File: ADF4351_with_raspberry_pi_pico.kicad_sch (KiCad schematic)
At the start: 0 parts

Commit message: wip ディスプレイとの接続、PLLとの接続は確定。制御用のボタン部分の作成を要する。
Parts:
- added A1: RaspberryPi_Pico, Module:RaspberryPi_Pico_Common_Unspecified, symbol MCU_Module:RaspberryPi_Pico
- added J1, J3: B4B-XH-A_LF__SN_, digikey-footprints:PinHeader_1x4_P2.5mm_Drill1.1mm, symbol dk_Rectangular-Connectors-Headers-Male-Pins:B4B-XH-A_LF__SN_
- added J2: 302-S101, digikey-footprints:PinHeader_2x5_P2.54mm_Drill1.2mm, symbol dk_Rectangular-Connectors-Headers-Male-Pins:302-S101
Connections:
- new net +3.3V: A1.36 (3V3), J1.1, J2.2
- new net +5V: A1.40 (VBUS), J3.1
- new net CE: A1.7 (GPIO5), J2.3
- new net CLK: A1.4 (GPIO2), J2.7
- new net DAT: A1.5 (GPIO3), J2.6
- new net GND: A1.13 (GND), A1.18 (GND), A1.23 (GND), A1.28 (GND), A1.3 (GND), A1.38 (GND), A1.8 (GND), J1.2, J2.1, J2.4, J3.4
- new net I2C0_SCL: A1.22 (GPIO17), J1.3
- new net I2C0_SDA: A1.21 (GPIO16), J1.4
- new net LD: A1.11 (GPIO8), J2.9
- new net LE: A1.10 (GPIO7), J2.5
- new net MUX: A1.6 (GPIO4), J2.8
- new net PDR: A1.9 (GPIO6), J2.10
- new net UART0_RX: A1.2 (GPIO1), J3.3
- new net UART0_TX: A1.1 (GPIO0), J3.2

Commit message: 回路図完成
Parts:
- added J4: Conn_01x03_Socket, Connector_PinSocket_2.54mm:PinSocket_1x03_P2.54mm_Vertical, symbol Connector:Conn_01x03_Socket
- added J5: Conn_01x05_Socket, Connector_PinSocket_2.54mm:PinSocket_1x03_P2.54mm_Vertical, symbol Connector:Conn_01x05_Socket
- added R1, R2: NC, Resistor_SMD:R_0603_1608Metric_Pad0.98x0.95mm_HandSolder, symbol Device:R_Small
- added R3, R4, R5: 1k, Resistor_SMD:R_0603_1608Metric_Pad0.98x0.95mm_HandSolder, symbol Device:R_Small
- added R6: 10k, Resistor_SMD:R_0603_1608Metric_Pad0.98x0.95mm_HandSolder, symbol Device:R_Small
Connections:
- net +3.3V: now also R1.1, R2.1
- net +5V: now also J5.5 (Pin_5)
- net GND: now also J4.2 (Pin_2), R6.1
- net I2C0_SCL: now also R1.2
- net I2C0_SDA: now also R2.2
- net Encoder_A: now reaches A1.14 (GPIO10)
- net Encoder_A: now also J4.1 (Pin_1)
- net Encoder_B: now reaches A1.15 (GPIO11)
- net Encoder_B: now also J4.3 (Pin_3)
- net Encoder_PUSH: now reaches A1.24 (GPIO18)
- net Encoder_PUSH: now also J5.3 (Pin_3), R6.2
- net Encoder_LED_RED: now reaches A1.25 (GPIO19)
- net Encoder_LED_RED: now also R3.1
- net Encoder_LED_GREEN: now reaches A1.26 (GPIO20)
- net Encoder_LED_GREEN: now also R4.1
- net Encoder_LED_BLUE: now reaches A1.27 (GPIO21)
- net Encoder_LED_BLUE: now also R5.1
- new net: J5.1 (Pin_1), R3.2
- new net: J5.4 (Pin_4), R5.2
- new net: J5.2 (Pin_2), R4.2
- no-connect marks 0 -> 13
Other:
- note added: "プルアップ用 対象のモジュール基板にプルアップがある場合は付けない"
- note added: "５VじゃないとLEDを駆動出来ない。 ラズピコが耐える事に期待する"
- moved on the sheet: J1, J2, J3

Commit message: マウントホールを追加
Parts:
- added H1, H2, H3, H4: MountingHole_Pad_MP, MountingHole:MountingHole_3.2mm_M3_Pad_Via, symbol Mechanical:MountingHole_Pad_MP
- J5: footprint Connector_PinSocket_2.54mm:PinSocket_1x03_P2.54mm_Vertical -> Connector_PinSocket_2.54mm:PinSocket_1x05_P2.54mm_Vertical
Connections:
- net GND: now also H1.MP, H2.MP, H3.MP, H4.MP
- no-connect marks 13 -> 14

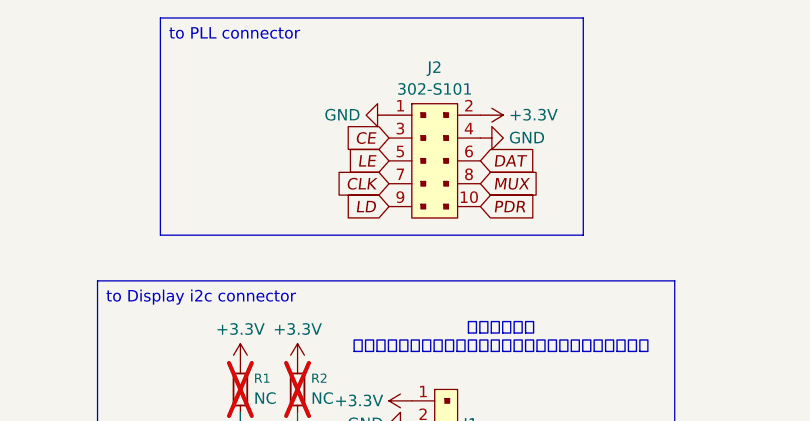
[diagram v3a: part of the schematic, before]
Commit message: fix 5*2 connector pin
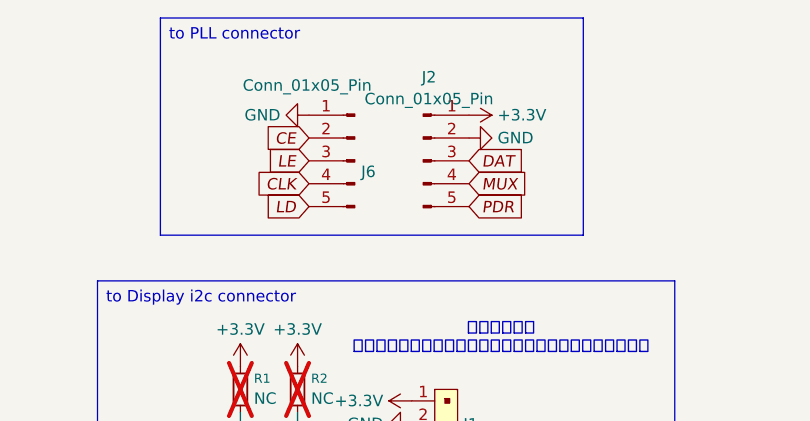
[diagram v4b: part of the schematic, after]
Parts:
- removed J2: 302-S101, digikey-footprints:PinHeader_2x5_P2.54mm_Drill1.2mm, symbol dk_Rectangular-Connectors-Headers-Male-Pins:302-S101
- added J2, J6: Conn_01x05_Pin, Connector_PinSocket_2.54mm:PinSocket_1x05_P2.54mm_Vertical, symbol Connector:Conn_01x05_Pin
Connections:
- net +3.3V: now also J2.1 (Pin_1)
- net CE: now also J6.2 (Pin_2)
- net CLK: now also J6.4 (Pin_4)
- net DAT: now also J2.3 (Pin_3)
- net GND: now also J2.2 (Pin_2), J6.1 (Pin_1)
- net LD: now also J6.5 (Pin_5)
- net LE: now also J6.3 (Pin_3)
- net MUX: now also J2.4 (Pin_4)
- net PDR: now also J2.5 (Pin_5)
